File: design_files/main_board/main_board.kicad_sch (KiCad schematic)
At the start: 49 parts, among them J1 Conn_01x32_Pin, J2 Conn_01x04_Male, J3 Conn_02x03_Odd_Even, J4 Jack-DC, J7 Conn_01x12_Male, SW1 SW_Push, SW2 SW_SPDT, U1 Z80CPU, U11 74LS74, U12 74LS32, U13 74LS374, U14 KM62256CLP, U15 DS1233, U2 KM62256CLP, U3 27256, U4 74LS00, U5 74LS04, U6 74LS138, U7 Z8440, U8 74LS74, U9 74LS161, X1 CXO_DIP8

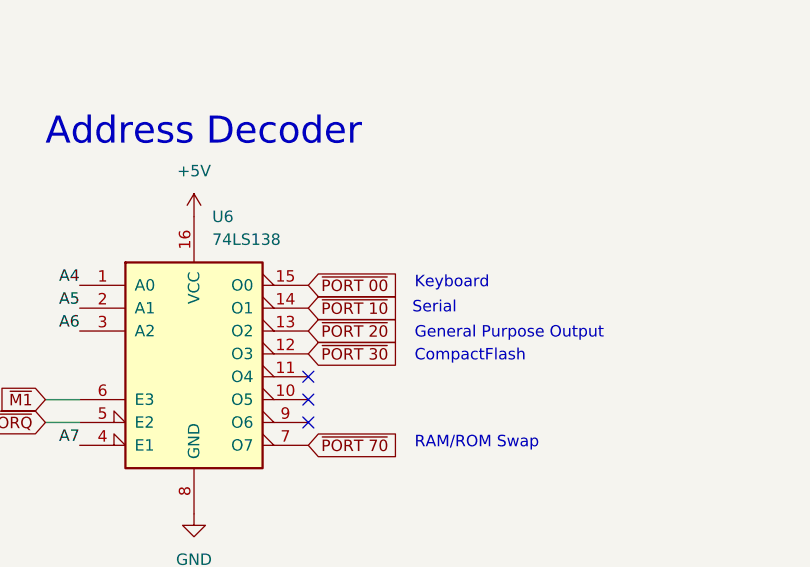
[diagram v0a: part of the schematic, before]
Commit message: More README
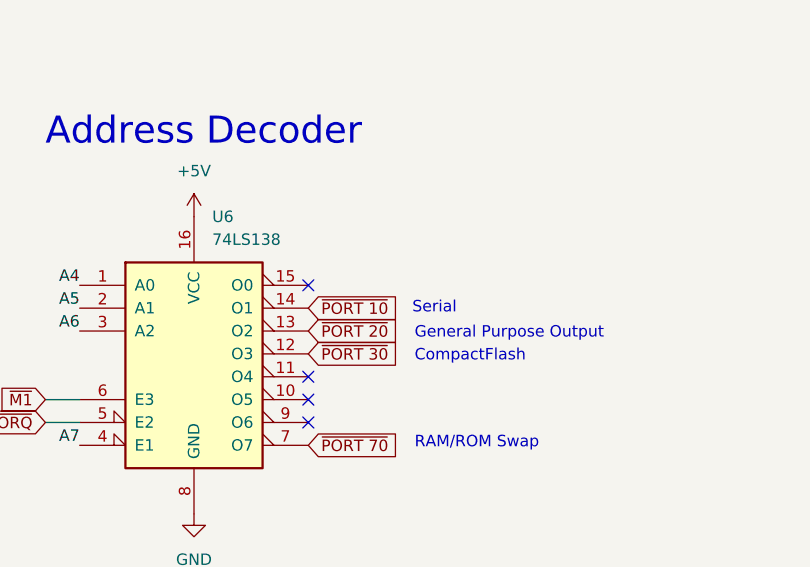
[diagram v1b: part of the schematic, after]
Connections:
- net ~{PORT 00}: no longer names the net of U6.15 (O0)
- no-connect marks 31 -> 32
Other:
- note removed: "Keyboard"
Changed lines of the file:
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@@
   (junction (at 235.585 391.16) (diameter 0) (color 0 0 0 0)
   )
+  (no_connect (at 242.443 160.274))
   (no_connect (at 543.306 289.814))
   (no_connect (at 214.63 84.455))
@@
     (effects (font (size 1.27 1.27)) (justify left bottom))
   )
-  (text "Keyboard" (at 254.254 160.782 0)
-    (effects (font (size 1.27 1.27)) (justify left bottom))
-  )
   (text "Low at startup" (at 360.299 353.441 0)
     (effects (font (size 1.27 1.27)) (justify left bottom))
@@
     )
   )
-  (global_label "~{PORT 00}" (shape input) (at 242.443 160.274 0) (fields_autoplaced)
-    (effects (font (size 1.27 1.27)) (justify left))
-    (property "Intersheetrefs" "${INTERSHEET_REFS}" (at 253.0809 160.1946 0)
-      (effects (font (size 1.27 1.27)) (justify left) hide)
-    )
-  )
